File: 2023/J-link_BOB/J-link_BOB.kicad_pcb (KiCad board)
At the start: 2 copper layers, 20.5 x 16.5 mm, 21 parts, among them J1 Conn_01x01_Female, J10 Conn_01x01_Female, J11 Conn_01x01_Female, J12 Conn_01x01_Female, J13 Conn_01x01_Female, J14 Conn_01x01_Female, J15 Conn_01x01_Female, J16 Conn_01x01_Female, J17 Conn_01x01_Female, J18 Conn_01x01_Female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

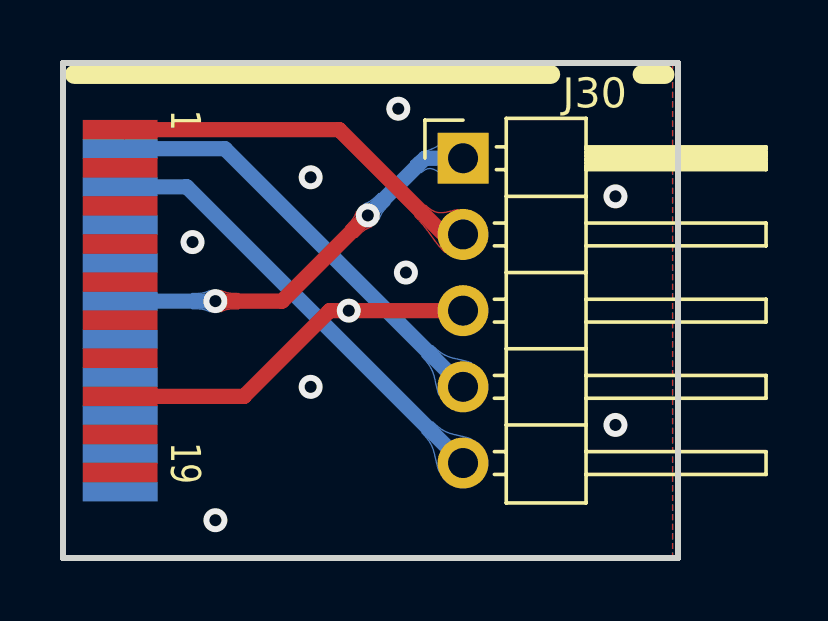
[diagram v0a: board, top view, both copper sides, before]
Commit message: Updated J-Link BOB with pin names
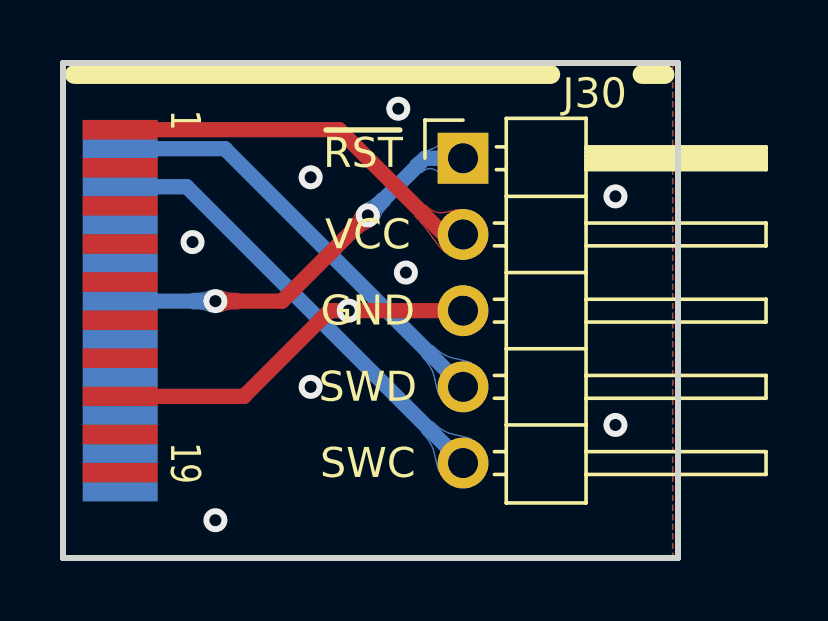
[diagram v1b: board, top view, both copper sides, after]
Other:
- board text added: "GND"
- board text added: "SWC"
- board text added: "SWD"
- board text added: "VCC"
- board text added: "~{RST}"
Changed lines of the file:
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@@
   (title_block
     (title "J-Link_BOB")
-    (date "2023-04-16")
+    (date "2023-04-27")
     (rev "A1")
     (company "MAG Laboratory")
@@
     (effects (font (size 1 0.8) (thickness 0.15)))
   )
+  (gr_text "VCC" (at 139.545 106.765) (layer "F.SilkS")
+    (effects (font (size 1 1) (thickness 0.18)))
+  )
+  (gr_text "SWD" (at 139.545 111.845) (layer "F.SilkS")
+    (effects (font (size 1 1) (thickness 0.18)))
+  )
   (gr_text "1" (at 133.449 102.955 270) (layer "F.SilkS")
     (effects (font (size 1 0.8) (thickness 0.15)))
   )
+  (gr_text "~{RST}" (at 139.385 104.05) (layer "F.SilkS")
+    (effects (font (size 1 1) (thickness 0.18)))
+  )
+  (gr_text "GND" (at 139.545 109.305) (layer "F.SilkS")
+    (effects (font (size 1 1) (thickness 0.18)))
+  )
+  (gr_text "SWC" (at 139.545 114.385) (layer "F.SilkS")
+    (effects (font (size 1 1) (thickness 0.18)))
+  )
   (segment (start 142.085 106.765) (end 138.5925 103.2725) (width 0.508) (layer "F.Cu") (net 1))
